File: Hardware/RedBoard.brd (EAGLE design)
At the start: 68.6 x 53.3 mm, 65 parts, among them IC3 LM1117, J2 ICSP, J3 POWER_JACKSUPER_BOMB_DIGITY, Q1 1A/60V/500mΩ, Q2 2N7002PW, U1 FT231XS, U2 MIC5205, U4 ATMEGA328P_TQFP, Y1 16MHz

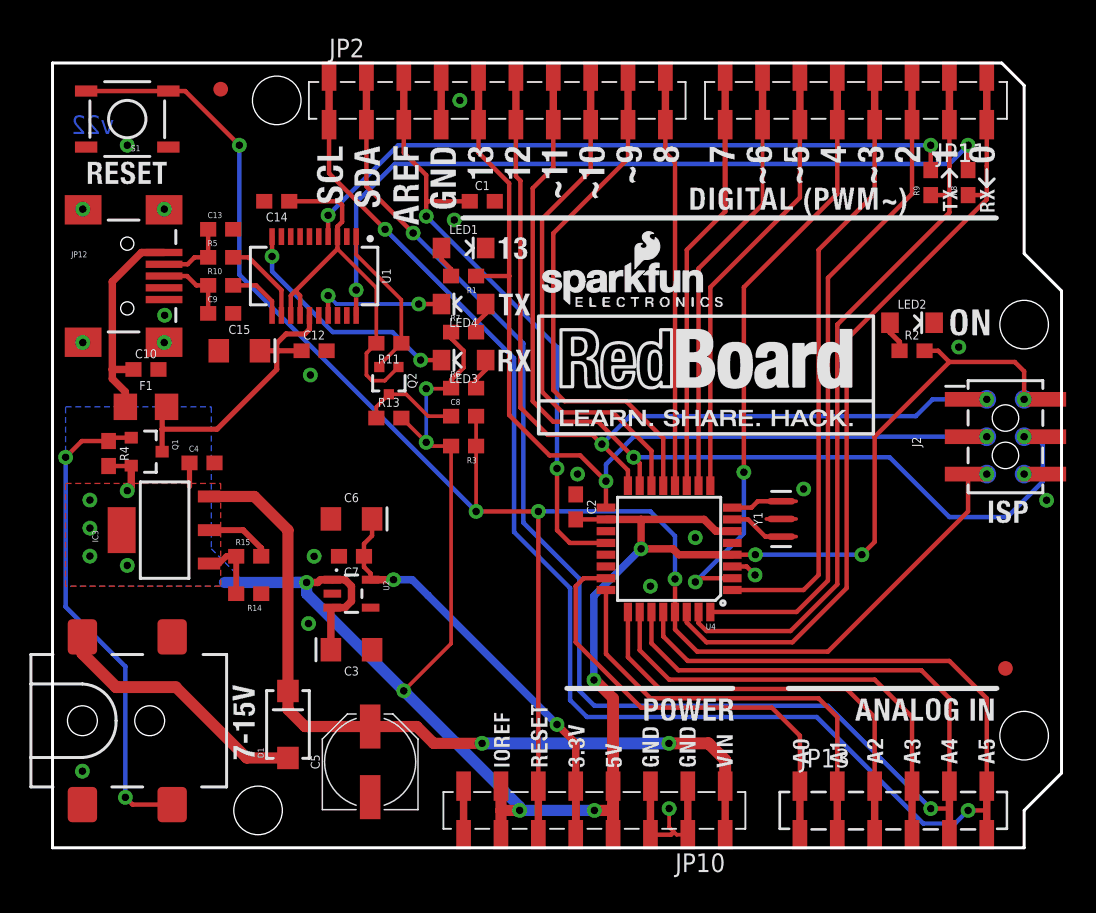
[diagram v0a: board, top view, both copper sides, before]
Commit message: Initial commit.
Changed USB. Added Qwiic. Added I/O jumper.
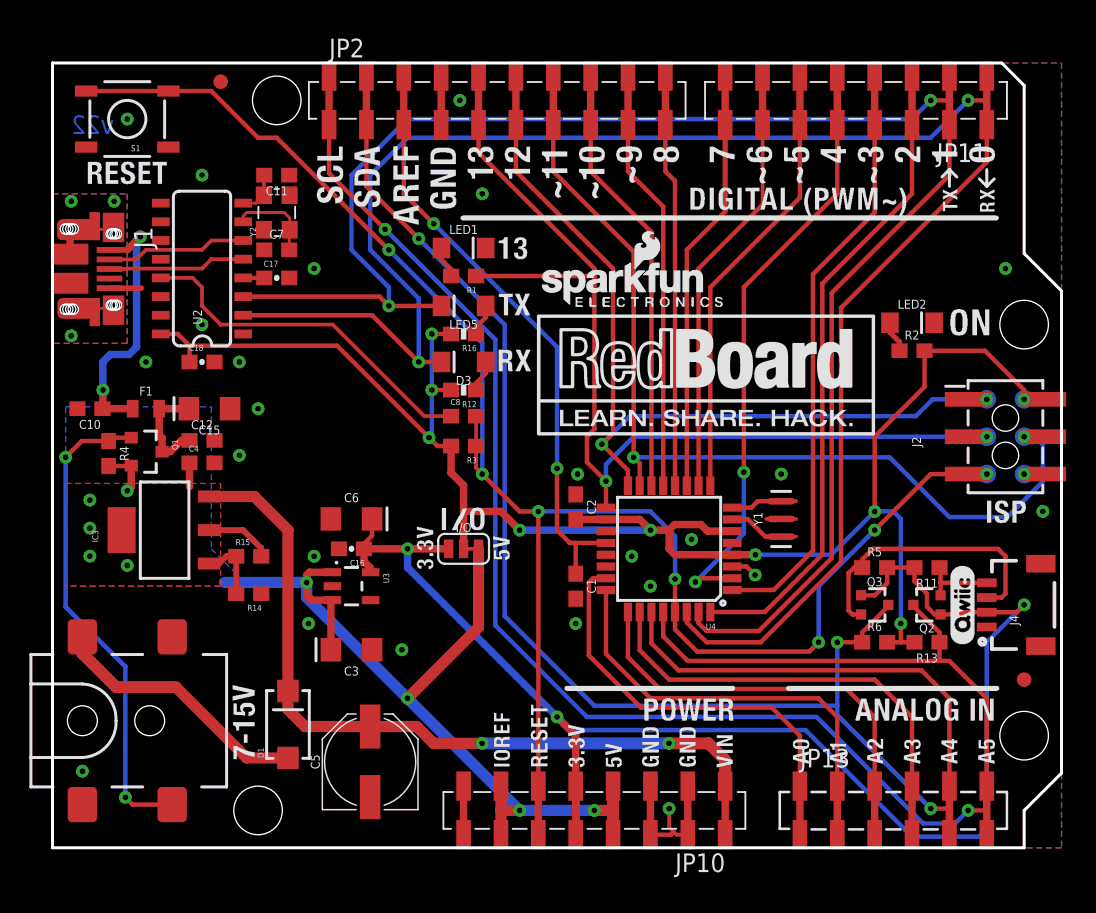
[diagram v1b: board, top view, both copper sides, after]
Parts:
- removed C13, C9: 47pF, SparkFun-Capacitors:0603
- removed C14: 0.1uF, SparkFun-Capacitors:0603
- removed FRAME2: FRAME-LETTER, SparkFun-Aesthetics:CREATIVE_COMMONS
- removed JP12: USB-MINIB-5PIN, SparkFun-Connectors:USB-MINIB
- removed LED3: Red, SparkFun-LED:LED-1206
- removed LED4: Yellow, SparkFun-LED:LED-1206
- removed R10: 27, SparkFun-Resistors:0603
- removed R7, R8, R9: 1k, SparkFun-Resistors:0603
- removed U1: FT231XS, SparkFun-IC-Comms:SSOP20_L
- added C11: 22pF, SparkFun-Capacitors:0603
- added C16: 1.0uF, SparkFun-Capacitors:0603-CAP
- added C17: 10nF, SparkFun-Capacitors:0603-CAP
- added C18: 0.1uF, SparkFun-Capacitors:0603-CAP
- added D3: Yellow, SparkFun-LED:LED-1206-HIDDENSILK
- added FRAME1: FRAME-LEDGER, SparkFun-Aesthetics:CREATIVE_COMMONS
- added I/O: (no value), SparkFun-Jumpers:SMT-JUMPER_3_1-NC_TRACE_SILK
- added J1: microB, SparkFun-Connectors:USB-MICROB-PTH
- added J4: SMD, SparkX:1X04_1MM_RA
- added LED5: GREEN, SparkFun-LED:LED-1206-HIDDENSILK
- added Q3: 2N7002PW, SparkFun-DiscreteSemi:SOT323
- added R12: 1K, SparkFun-Resistors:0603-RES
- added R16: 330, SparkFun-Resistors:0603-RES
- added U$2: (no value), Labels-0_04:(QWIIC)
- added U3: AP2112-3.3V, SparkFun-PowerIC:SOT23-5
- added Y2: 12MHz, USB Basic:CRYSTAL-SMD-3.2X2.5
- C7: value 1.0uF -> 22pF
- F1: value 6V/0.5A -> PPTC_6V500MA; device SparkFun-Fuses:1206 -> SparkFun-Fuses:0805
- JP10: value JP10 -> (none)
- JP11: value IOL -> JP11
- JP13: value AD -> (none)
- LED1: device SparkFun-LED:LED-1206 -> SparkFun-LED:LED-1206-HIDDENSILK
- LED2: value Green -> GREEN; device SparkFun-LED:LED-1206 -> SparkFun-LED:LED-1206-HIDDENSILK
- R11, R13: value 10k -> 2.2k
- R5: value 27 -> 2.2k
- R6: value 1k -> 2.2k
- U2: value MIC5205 -> CH340G; device SparkFun-PowerIC:SOT23-5 -> SparkFun-DigitalIC:SO016
- moved R5 49.2 mm to (55.9, 19.1)
- moved Q2 39.6 mm to (59.4, 16.5), turned to 90 degrees
- moved R11 39.6 mm to (59.4, 19.1)
- moved R13 39.6 mm to (59.4, 14.0), turned to 180 degrees
- moved R6 32.8 mm to (55.9, 14.0)
- moved C1 26.9 mm to (35.6, 17.8), turned to 270 degrees
- moved U2 24.3 mm to (10.2, 39.4), turned to 90 degrees
- moved C7 21.4 mm to (15.2, 40.6), turned to 0 degrees
- moved C12 9.76 mm to (10.2, 27.7)
- moved C10 4.65 mm to (2.54, 29.8), turned to 180 degrees
- moved C15 4.43 mm to (10.7, 29.8), turned to 180 degrees
- moved JP8 1.48 mm to (66.0, 11.4)
- moved JP9 0.51 mm to (11.4, 52.1)
- moved F1 0.13 mm to (6.35, 29.8)
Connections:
- removed net 3.3V_F: C14.1, Q2.1, R11.2, U1.13, U1.14, U1.3
- removed net D+: C9.1, JP12.D+, R10.1
- removed net D-: C13.1, JP12.D-, R5.1
- removed net DTR: C8.1, Q2.3, R13.1
- removed net FTDI_DTR: Q2.2, R11.1, U1.1
- removed net N$10: LED4.A, R7.2
- removed net N$6: R5.2, U1.12
- removed net N$7: R10.2, U1.11
- removed net N$8: LED3.A, R6.2
- removed net RXD: R9.2, U1.4
- removed net RXLED: LED4.C, U1.17
- removed net TXD: R8.2, U1.20
- removed net TXLED: LED3.C, U1.10
- new net !DTR: C8.1, U2.13
- new net LV_SCL: J4.4, Q2.2, R11.1
- new net LV_SDA: J4.3, Q3.2, R5.1
- new net N$11: C11.2, U2.8, Y2.3
- new net N$12: C7.2, U2.7, Y2.1
- new net N$13: J1.D-, U2.6
- new net N$14: J1.D+, U2.5
- new net N$5: LED5.A, R16.1
- new net N$9: D3.A, R12.1
- new net SHLD: J1.7, J1.SHEILD2, J1.SHIELD, J1.SHIELD10, J1.SHIELD11, J1.SHIELD12, J1.SHIELD3, J1.SHIELD4, J1.SHIELD5, J1.SHIELD6, J1.SHIELD8, J1.SHIELD9
- new net V3: C17.1, U2.4
- new net VCC: C18.1, C2.2, I/O.2, J2.2, R12.2, R13.2, R16.2, R2.2, R3.2, R6.2, TP1.P$1, U2.16, U4.18, U4.4, U4.6
- net 3.3V: now also C16.1, I/O.1, J4.2, Q2.1, Q3.1, R11.2, R5.2, U3.5; no longer C7.1, U2.5
- net 5V: now also I/O.3, U3.1, U3.3; no longer C2.2, J2.2, R13.2, R2.2, R3.2, R6.1, R7.1, TP1.P$1, U2.1, U2.3, U4.18, U4.4, U4.6
- net AD4/SDA: now also Q3.3, R6.1
- net AD5/SCL: now also Q2.3, R13.1
- net GND: now also C11.1, C16.2, C17.2, C18.2, C7.1, J1.GND, J4.1, U2.1, U3.2, Y2.2, Y2.4; no longer C13.2, C14.2, C7.2, C9.2, JP12.GND, JP12.MTN1, JP12.MTN2, JP12.MTN3, JP12.MTN4, U1.16, U1.6, U2.2
- net RX-I: now also D3.C, U2.2; no longer R8.1
- net TX-O: now also LED5.C, U2.3; no longer R9.1
- net USBVCC: no longer U1.15
- net VUSB: now also J1.VBUS; no longer JP12.VBUS
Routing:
- net VCC: track 0.00 -> 116.5 mm, vias 0 -> 9
- net 5V: track 167.1 -> 74.7 mm, vias 16 -> 9
- net RX-I: track 50.4 -> 122.4 mm, vias 0 -> 2
- net 3.3V: track 29.3 -> 98.2 mm, vias 2 -> 3
- net TX-O: track 50.7 -> 112.9 mm, vias 0 -> 2
- net TXD: track 52.6 -> 0.00 mm, vias 2 -> 0
- net RXD: track 46.1 -> 0.00 mm, vias 2 -> 0
- net 3.3V_F: track 27.1 -> 0.00 mm
- net !DTR: track 0.00 -> 24.4 mm
- net LV_SDA: track 0.00 -> 19.3 mm
- net TXLED: track 16.4 -> 0.00 mm, vias 2 -> 0
- net USBVCC: track 20.8 -> 7.26 mm
- net FTDI_DTR: track 10.8 -> 0.00 mm
- net AD4/SDA: track 106.1 -> 115.8 mm, vias 2 -> 3
- net N$13: track 0.00 -> 9.62 mm
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- added copper zone on layer 1, net SHLD
- added copper zone on layer 16, net SHLD
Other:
- board text added: "Based on Arduino by: M. Banzi, D. Cuartielles, T. Igoe, G. Martino, D. Mellis"
- board text added: "J. Lindblom, N. Seidle"
- board text removed: "Based on Arduino by: M.Banzi, D.Cuartielles, T.Igoe, G.Martino, D.Mellis"
- board text removed: "J.Lindblom"
